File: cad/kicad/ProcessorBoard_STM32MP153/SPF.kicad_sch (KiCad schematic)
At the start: 1 part, among them J2 SFP

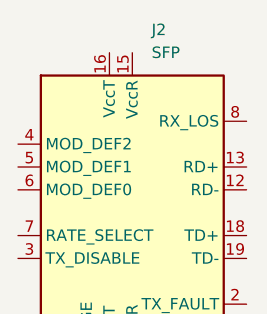
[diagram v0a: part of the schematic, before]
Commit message: piddling with power
11 distinct power nets out :vine_boom:
5V@8A in :vine_boom:
3v3@3A in :vine_boom:
secure os i2c :vine_boom:

:vine_boom:
:vine_boom:
release me
:vine_boom:

these are absolute maximums the PMIC will need, shouldnt get near them unless the outputs shorted. big step up from the dinky 3v3 mcus :(
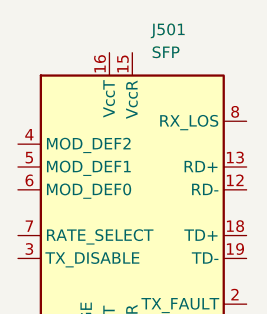
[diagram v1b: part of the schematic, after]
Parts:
- renumbered J2 to J501
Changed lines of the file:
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@@
 		(dnp no)
 		(fields_autoplaced yes)
-		(property "Reference" "J2"
+		(property "Reference" "J501"
 			(at 116.4433 72.39 0)
 			(show_name no)
@@
 			(project "ProcessorBoard_STM32MP153"
 				(path "/e63e39d7-6ac0-4ffd-8aa3-1841a4541b55/9bbfbe68-2804-40ed-9d5f-0570a6a580b2"
-					(reference "J2")
+					(reference "J501")
 					(unit 1)
 				)

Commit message: is this tuff
most datasheets from LCSC are "not for public release"
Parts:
- J501: footprint Connector:Connector_SFP_and_Cage -> __WM_Local:Connector_SFP_and_Cage; Field6 (none) -> https://www.mouser.com/en/ProductDetail/Amphenol-Commercial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; mouser (none) -> https://www.mouser.com/en/ProductDetail/Pulse-Electronics/E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; unit x1 (none) -> 5.0
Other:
- note added: "JLC SFP design duide"
- note added: "is this tuff"
- moved on the sheet: J501

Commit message: crab company
the lion does not concern himself with radiation
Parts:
- added X501: RTL8211FS(I)-xx-xx, Package_DFN_QFN:QFN-48-1EP_6x6mm_P0.4mm_EP4.2x4.2mm, symbol __WM_Local:RTL8211FS(I)-xx-xx
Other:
- moved on the sheet: J501

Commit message: big ol kicad file ?
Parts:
- added C501, C502, C504: 4.7u, Capacitor_SMD:C_01005_0402Metric_Pad0.57x0.30mm_HandSolder, symbol Device:C_Small
- added C503: 100n, Capacitor_SMD:C_0402_1005Metric_Pad0.74x0.62mm_HandSolder, symbol Device:C_Small
- added L501: 2.2u, Inductor_SMD:L_Ferrocore_DLG-0302, symbol Device:L_Small
- added R501, R502: 1.2k, Resistor_SMD:R_0603_1608Metric_Pad0.98x0.95mm_HandSolder, symbol Device:R_Small_US
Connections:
- net GND: now reaches J501.1 (VeeT), J501.17 (VeeT), J501.20 (VeeT)
- net GND: now also J501.10 (VeeR), J501.11 (VeeR), J501.14 (VeeR), J501.9 (VeeR), X501.49 (GND), C501.1, C502.2, C503.2, C504.2
- net RD-: now reaches J501.12 (RD-)
- net RD+: now reaches J501.13 (RD+)
- net SPF_PWR_3v3: now reaches J501.15 (VccR)
- net SPF_PWR_3v3: now also J501.16 (VccT), X501.1 (AV_{dd}3v3), X501.12 (AV_{dd}3v3), X501.30 (AV_{dd}3v3), X501.31 (V_{dd}_REG), C501.2, C504.1, R501.1, R502.1
- net TD+: now reaches J501.18 (TD+)
- net TD-: now reaches J501.19 (TD-)
- net MOD_SDA: now reaches J501.4 (MOD_DEF2)
- net MOD_SDA: now also R501.2
- net MOD_SCL: now reaches J501.5 (MOD_DEF1)
- net MOD_SCL: now also R502.2
- net MOD_PRZ: now reaches J501.6 (MOD_DEF0)
- net at X501.22 (DV_{dd}1v0): now also X501.4 (AV_{dd}1v0), X501.47 (DV_{dd}1v0), X501.9 (AV_{dd}1v0), C502.1, C503.1, L501.2
- net at X501.32 (REG_OUT): now also L501.1
- net xtal_in: now reaches X501.45 (XTAL_IN)
- net xtal_out: now reaches X501.46 (XTAL_OUT)
- net reset: now reaches X501.48 (RSET)
- no-connect marks 0 -> 1
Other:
- note added: "design guide of SOMEWHAT related Realtek IC"
- moved on the sheet: J501, X501

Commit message: realtek bridge thing somewhat more wired
apparently the proper term for via skimping and what not is NFPR (non functional pad removal). all my homies love NFPR. so it is possible to route 0.5mm bga. still fighting the dog but at least cant bring it to another layer
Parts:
- added C505: 100n, Capacitor_SMD:C_0402_1005Metric_Pad0.74x0.62mm_HandSolder, symbol Device:C_Small
- added D501, D503: LED_KRGB, LED_SMD:LED_Cree-PLCC4_2x2mm_CW, symbol Device:LED_KRGB
- added Q501: MMBTA92, Package_TO_SOT_SMD:SOT-23, symbol Transistor_BJT:MMBTA92
- added Q502: MMBT5551L, Package_TO_SOT_SMD:SOT-23, symbol Transistor_BJT:MMBT5551L
- added R503, R506, R507, R508, R509: 330, Resistor_SMD:R_0603_1608Metric_Pad0.98x0.95mm_HandSolder, symbol Device:R_Small_US
- added R504, R505: 10k, Resistor_SMD:R_0603_1608Metric_Pad0.98x0.95mm_HandSolder, symbol Device:R_Small_US
- added U502: DSC6101HL3B-025.0000, Package_LGA:VLGA-4_2x2.5mm_P1.65mm, symbol __WM_Local:DSC6101HL3B-025.0000
- R501, R502: value 1.2k -> 5.6k; footprint Resistor_SMD:R_0603_1608Metric_Pad0.98x0.95mm_HandSolder -> Resistor_SMD:R_0805_2012Metric_Pad1.20x1.40mm_HandSolder; mouser https://www.mouser.com/en/ProductDetail/TE-Connectivity-Hol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 -> https://www.mouser.com/en/ProductDetail/KOA-Speer/RK73H2ATT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; unit x1 0.10 -> 0.1; unit x10 0.018 -> 0.021
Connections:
- net RD+ is gone; now on an unnamed net: J501.13 (RD+)
- net RD- is gone; now on an unnamed net: J501.12 (RD-)
- net TD+ is gone; now on an unnamed net: J501.18 (TD+)
- net TD- is gone; now on an unnamed net: J501.19 (TD-)
- net GND: now also X501.45 (XTAL_IN), C505.1, D501.1 (K), D503.1 (K), U502.2 (GND)
- net MOD_PRZ: now also R504.2
- net SPF_PWR_3v3: now also C505.2, Q501.2 (E), Q502.3 (C), R504.1, R505.1, U502.1 (OE), U502.4 (V_{DD})
- net xtal_in: now also U502.3 (OUT); no longer X501.45 (XTAL_IN)
- net tx_fault: now reaches J501.2 (TX_FAULT)
- net tx_fault: now also Q502.1 (B), R505.2
- net TX_DISABLE: now reaches J501.3 (TX_DISABLE)
- net TX_DISABLE: now also R509.1
- net LED_{1}: now reaches X501.36 (LED_{1})
- net LED_{1}: now also Q501.1 (B)
- net LED_{2}: now reaches X501.37 (LED_{2})
- net LED_{2}: now also R503.1, R508.1
- new net: Q501.3 (C), R507.1
- new net: Q502.2 (E), R506.1
- new net: D501.2 (RA), R506.2
- new net: D501.4 (BA), R509.2
- new net: D503.2 (RA), R508.2
- new net: D503.3 (GA), R507.2
- new net: D503.4 (BA), R503.2
- no-connect marks 1 -> 11
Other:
- note added: "JLC design guide"
- note added: "MDIO addr"
- note added: "SFP MSA PU: 4.7k - 10k"
- note added: "TODO: figure out the RXD lines D: theyre multi-purpose"
- note added: "bridge IC datasheet"
- note added: "mode 001: FIBER <-> RGMII"
- note added: "pg.4 of bridge datasheet"
- moved on the sheet: C501, C502, C503, C504, J501, L501, X501

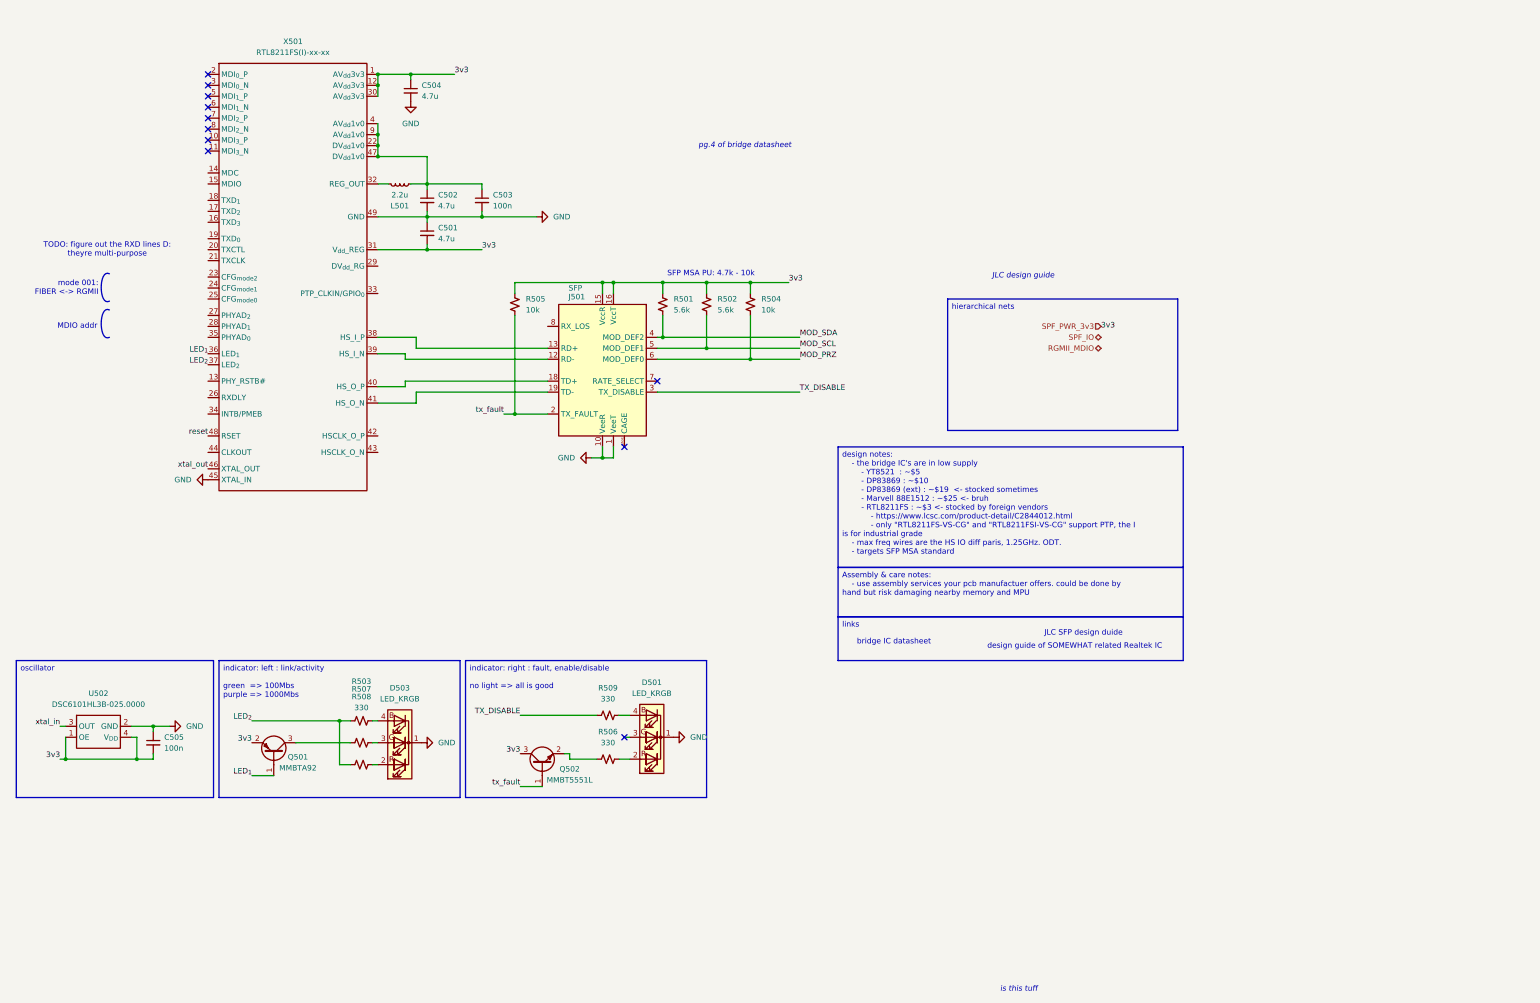
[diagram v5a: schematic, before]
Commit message: double inversion trap
the crab has a double inversion, the pins internal logic is inverted. and the output logic-high is dynamically determined. bruh
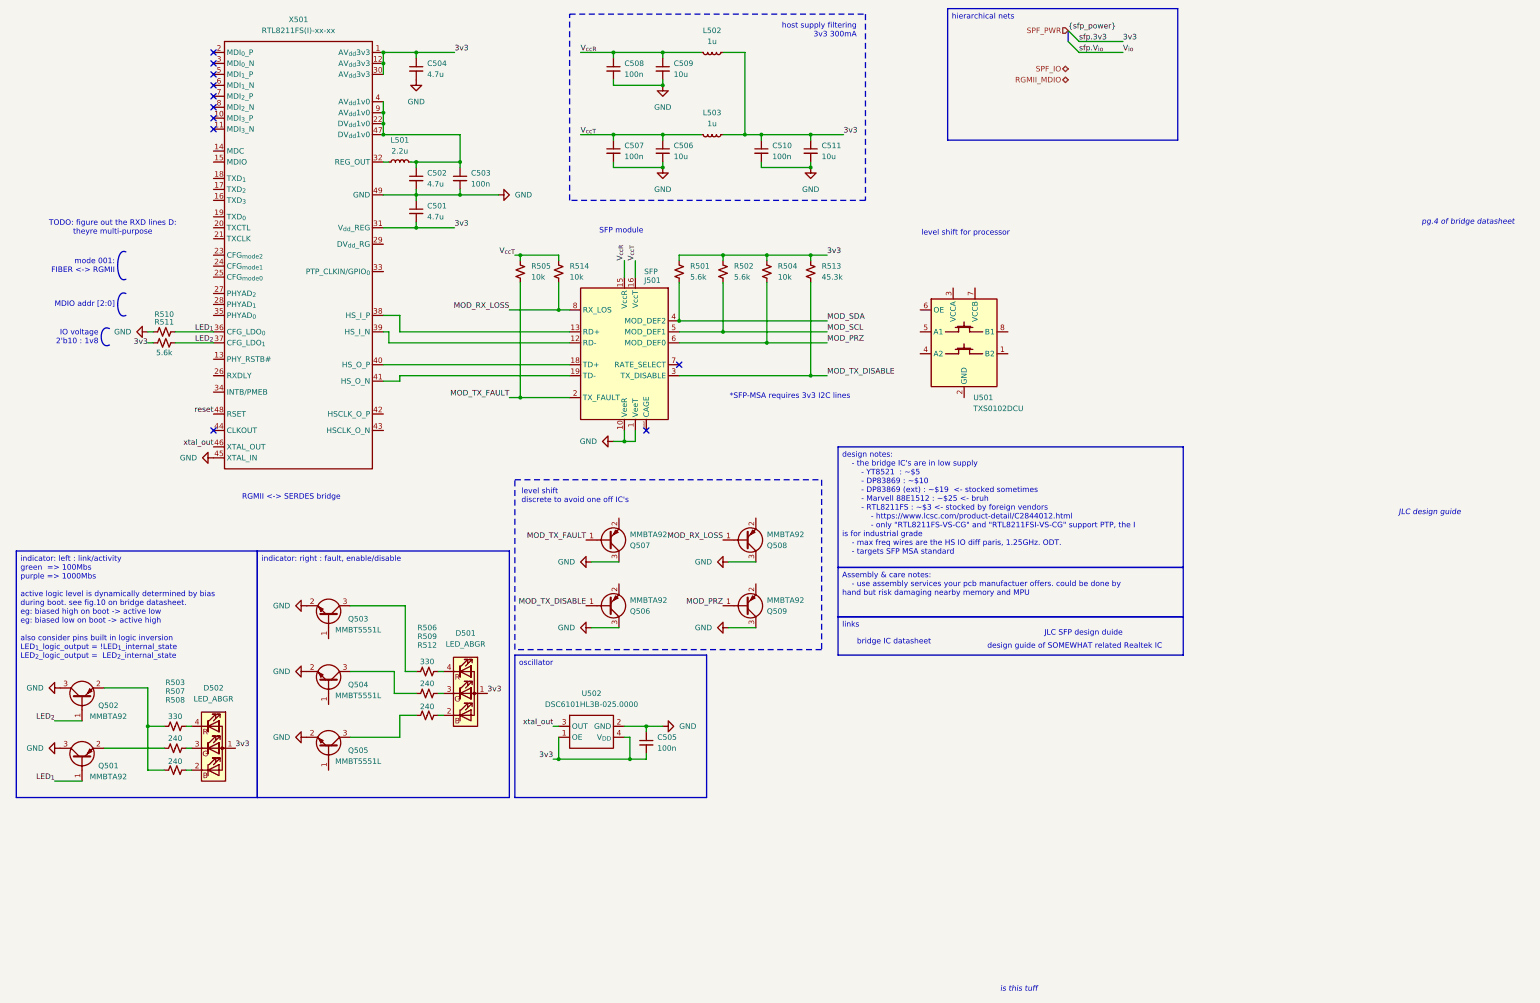
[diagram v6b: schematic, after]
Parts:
- removed D501, D503: LED_KRGB, LED_SMD:LED_Cree-PLCC4_2x2mm_CW, symbol Device:LED_KRGB
- removed Q502: MMBT5551L, Package_TO_SOT_SMD:SOT-23, symbol Transistor_BJT:MMBT5551L
- added C506, C509, C511: 10u, Capacitor_SMD:C_0603_1608Metric_Pad1.08x0.95mm_HandSolder, symbol Device:C_Small
- added C507, C508, C510: 100n, Capacitor_SMD:C_0402_1005Metric_Pad0.74x0.62mm_HandSolder, symbol Device:C_Small
- added D501, D502: LED_ABGR, symbol Device:LED_ABGR
- added L502, L503: 1u, Inductor_SMD:L_1008_2520Metric_Pad1.43x2.20mm_HandSolder, symbol Device:L_Small
- added Q502, Q506, Q507, Q508, Q509: MMBTA92, Package_TO_SOT_SMD:SOT-23, symbol Transistor_BJT:MMBTA92
- added Q503, Q504, Q505: MMBT5551L, Package_TO_SOT_SMD:SOT-23, symbol Transistor_BJT:MMBT5551L
- added R510, R511: 5.6k, Resistor_SMD:R_0805_2012Metric_Pad1.20x1.40mm_HandSolder, symbol Device:R_Small_US
- added R512: 240, Capacitor_SMD:C_0402_1005Metric_Pad0.74x0.62mm_HandSolder, symbol Device:R_Small_US
- added R513: 45.3k, Resistor_SMD:R_0603_1608Metric_Pad0.98x0.95mm_HandSolder, symbol Device:R_Small_US
- added R514: 10k, Resistor_SMD:R_0603_1608Metric_Pad0.98x0.95mm_HandSolder, symbol Device:R_Small_US
- added U501: TXS0102DCU, Package_SO:VSSOP-8_2.3x2mm_P0.5mm, symbol Logic_LevelTranslator:TXS0102DCU
- R507, R508, R509: value 330 -> 240; footprint Resistor_SMD:R_0603_1608Metric_Pad0.98x0.95mm_HandSolder -> Capacitor_SMD:C_0402_1005Metric_Pad0.74x0.62mm_HandSolder; mouser https://www.mouser.com/en/ProductDetail/Bourns/CR0603-FX-33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 -> https://www.mouser.com/en/ProductDetail/Susumu/RR0510P-241-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; unit x10 0.012 -> 0.023; unit x100 (none) -> 0.022
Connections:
- net xtal_in is gone; now on net xtal_out: U502.3 (OUT)
- net GND: now also Q501.3 (C), C506.2, C507.2, C508.2, C509.2, C510.2, C511.2, Q502.3 (C), Q503.2 (E), Q504.2 (E), Q505.2 (E), Q506.3 (C), Q507.3 (C), Q508.3 (C), Q509.3 (C), R510.1
- net LED_{1}: now also R510.2
- net LED_{2}: now also Q502.1 (B), R511.2; no longer R503.1, R508.1
- net MOD_PRZ: now also Q509.1 (B)
- net MOD_SDA: now also R501.1; no longer R501.2
- net at R507.1: now also Q501.2 (E); no longer Q501.3 (C)
- net at R506.1: now also Q503.3 (C)
- net at R506.2: now also D501.4 (RK)
- net at R509.2: now also D501.3 (GK)
- net at R508.2: now also D502.2 (BK)
- net at R507.2: now also D502.3 (GK)
- net at R503.2: now also D502.4 (RK)
- net MOD_RX_LOSS: now reaches J501.8 (RX_LOS)
- net MOD_RX_LOSS: now also Q508.1 (B), R514.2
- net SPF_PWR_3v3 renamed 3v3
- net 3v3: now also R501.2, C510.1, C511.1, D501.1 (A), D502.1 (A), L502.1, L503.1, R511.1, R513.1; no longer J501.15 (VccR), J501.16 (VccT), Q501.2 (E), R501.1, R505.1
- net TX_DISABLE: no longer names the net of R509.1
- net TX_DISABLE: now also Q504.3 (C); no longer J501.3 (TX_DISABLE)
- net tx_fault renamed MOD_TX_FAULT
- net MOD_TX_FAULT: now also Q507.1 (B)
- new net: Q502.2 (E), R503.1, R508.1
- new net: Q505.3 (C), R512.1
- new net: D501.2 (BK), R512.2
- new net MOD_TX_DISABLE: J501.3 (TX_DISABLE), Q506.1 (B), R513.2
- new net V_{ccR}: C508.1, C509.1, J501.15 (VccR), L502.2
- new net V_{ccT}: C506.1, C507.1, J501.16 (VccT), L503.2, R505.1, R514.1
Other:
- note added: "*SFP-MSA requires 3v3 I2C lines"
- note added: "IO voltage 2'b10 : 1v8"
- note added: "MDIO addr [2:0]"
- note added: "RGMII <-> SERDES bridge"
- note added: "SFP module"
- note added: "host supply filtering 3v3 300mA"
- note added: "level shift discrete to avoid one off IC's"
- note added: "level shift for processor"
- note removed: "MDIO addr"
- note removed: "SFP MSA PU: 4.7k - 10k"
- moved on the sheet: C501, C502, C503, C504, C505, J501, L501, R501, R502, R504, R505, U502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

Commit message: all hail the auto router
https://ih1.redbubble.net/image.6083290940.2638/flat,750x,075,f-pad,750x1000,f8f8f8.jpg
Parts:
- removed Q501, Q506: MMBTA92, Package_TO_SOT_SMD:SOT-23, symbol Transistor_BJT:MMBTA92
- added C512, C513: 100n, Capacitor_SMD:C_0402_1005Metric_Pad0.74x0.62mm_HandSolder, symbol Device:C_Small
- added Q501, Q506: MMBT5551L, Package_TO_SOT_SMD:SOT-23, symbol Transistor_BJT:MMBT5551L
- C501, C502, C504: footprint Capacitor_SMD:C_01005_0402Metric_Pad0.57x0.30mm_HandSolder -> Capacitor_SMD:C_0402_1005Metric_Pad0.74x0.62mm_HandSolder
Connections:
- net 3v3: now also U501.7 (VCCB), C512.1
- net GND: now also U501.2 (GND), C512.2, C513.2, Q501.2 (E), Q506.2 (E)
- net LED_{1}: now also Q501.1 (B)
- net MOD_SCL: now also U501.1 (B2)
- net MOD_SDA: now also U501.8 (B1)
- net MOD_TX_DISABLE: now also Q506.3 (C)
- net V_{io}: now also U501.3 (VCCA), U501.6 (OE), C513.1
- net at R507.1: now also Q501.3 (C)
- net spfio.SCL: now reaches U501.4 (A2)
- net spfio.SDA: now reaches U501.5 (A1)
- net spfio.module.rx_loss: now reaches Q508.2 (E)
- net spfio.led_{green}: now reaches Q504.1 (B)
- net spfio.module.present: now reaches Q509.2 (E)
- net spfio.led_{blue}: now reaches Q505.1 (B)
- net spfio.led_{red}: now reaches Q503.1 (B)
- net spfio.module.tx_fault: now reaches Q507.2 (E)
- new net spfio.module.tx_disable: Q506.1 (B)
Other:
- moved on the sheet: C505, C506, C507, C508, C509, C510, C511, L502, L503, Q507, Q508, Q509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

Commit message: somewhat fanned
the auto router sucks :( . and the auto fanout sucks. and i routed everything on the wrong grid and it snapped to teh wrong places and i only noticed most of teh way though so i push and make it tomorrows problem
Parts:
- renumbered C504 to C501, C501 to C503, C503 to C504, C508 to C506, C509 to C508, C506 to C509, C513 to C512, C512 to C513, D502 to D501, D501 to D502, Q502 to Q501, Q501 to Q502, Q507 to Q506, Q506 to Q507, R510 to R501, R511 to R502, R507 to R504, R508 to R505, R509 to R507, R512 to R508, R505 to R509, R514 to R510, R501 to R511, R502 to R512, R504 to R513, R513 to R514, U502 to U501, U501 to U502
